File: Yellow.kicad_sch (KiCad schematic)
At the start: 15 parts

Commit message: Rename Amber to Yellow everywhere
Signed-off-by: Stefan Agner <stefan@agner.ch>
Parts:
- H5, H6: footprint Amber:DrillSlot_Plated_3.5x2.5mm -> Yellow:DrillSlot_Plated_3.5x2.5mm
- HS1: footprint Amber:Heatsink_56x56mm_2xFixation3.2mm -> Yellow:Heatsink_56x56mm_2xFixation3.2mm
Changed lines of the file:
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@@
       (effects (font (size 1.27 1.27)) (justify left))
     )
-    (property "Footprint" "Amber:DrillSlot_Plated_3.5x2.5mm" (id 2) (at 111.76 182.88 0)
+    (property "Footprint" "Yellow:DrillSlot_Plated_3.5x2.5mm" (id 2) (at 111.76 182.88 0)
       (effects (font (size 1.27 1.27)) hide)
     )
@@
       (effects (font (size 1.27 1.27)) (justify left))
     )
-    (property "Footprint" "Amber:DrillSlot_Plated_3.5x2.5mm" (id 2) (at 111.76 190.5 0)
+    (property "Footprint" "Yellow:DrillSlot_Plated_3.5x2.5mm" (id 2) (at 111.76 190.5 0)
       (effects (font (size 1.27 1.27)) hide)
     )
@@
       (effects (font (size 1.27 1.27)) (justify left))
     )
-    (property "Footprint" "Amber:Heatsink_56x56mm_2xFixation3.2mm" (id 2) (at 133.6548 185.42 0)
+    (property "Footprint" "Yellow:Heatsink_56x56mm_2xFixation3.2mm" (id 2) (at 133.6548 185.42 0)
       (effects (font (size 1.27 1.27)) hide)
     )
@@
     )
     (path "/6888556d-e390-44b5-977e-8a0092745a4b/59b3b2a4-69cc-4b91-a496-9a2aacf0b558"
-      (reference "FL1") (unit 1) (value "1k@100MHz{slash}500mA") (footprint "Amber:L_CommonModeChoke_Murata_DLW5B")
+      (reference "FL1") (unit 1) (value "1k@100MHz{slash}500mA") (footprint "Yellow:L_CommonModeChoke_Murata_DLW5B")
     )
     (path "/13673698-1ae8-48ac-89ad-67bec4817dbe"
@@
     )
     (path "/37de04fb-2d22-493d-a648-e024c9d5a4fc"
-      (reference "H5") (unit 1) (value "MountingHole") (footprint "Amber:DrillSlot_Plated_3.5x2.5mm")
+      (reference "H5") (unit 1) (value "MountingHole") (footprint "Yellow:DrillSlot_Plated_3.5x2.5mm")
     )
     (path "/bfcec0b4-32c4-4ebf-8bb4-4766287797f1"
-      (reference "H6") (unit 1) (value "MountingHole") (footprint "Amber:DrillSlot_Plated_3.5x2.5mm")
+      (reference "H6") (unit 1) (value "MountingHole") (footprint "Yellow:DrillSlot_Plated_3.5x2.5mm")
     )
     (path "/cd73f910-31d6-4226-a110-18f09eef8514"
-      (reference "HS1") (unit 1) (value "Heatsink") (footprint "Amber:Heatsink_56x56mm_2xFixation3.2mm")
+      (reference "HS1") (unit 1) (value "Heatsink") (footprint "Yellow:Heatsink_56x56mm_2xFixation3.2mm")
     )
     (path "/c7bf4e1f-6bd1-4be7-9e56-1bd438bf5d42/eda8ae3b-dbdd-4e73-8dc6-e01177bfb4f7"
-      (reference "J1") (unit 1) (value "Barrel_Jack") (footprint "Amber:BarrelJack_CUI_PJ-002A")
+      (reference "J1") (unit 1) (value "Barrel_Jack") (footprint "Yellow:BarrelJack_CUI_PJ-002A")
     )
     (path "/18c18357-12fa-4472-a108-e954e5bd7840/6dd5e861-e5d4-4759-b127-4958e3f04beb"
-      (reference "J2") (unit 1) (value "RJ45_LINK-PP_LPJG0926HENL_Horizontal") (footprint "Amber:RJ45_LINK-PP_LPJG0926HENL_Horizontal")
+      (reference "J2") (unit 1) (value "RJ45_LINK-PP_LPJG0926HENL_Horizontal") (footprint "Yellow:RJ45_LINK-PP_LPJG0926HENL_Horizontal")
     )
     (path "/aa1d8d83-5167-420c-9ee7-3e4dcc942bfc/e0469852-771a-434b-963a-8ecb4c38b617"
@@
     )
     (path "/a9e0a5b9-8f0f-46f3-b2b0-a429c678afed/45c3bea5-38ff-4276-ad09-4c18c95d656c"
-      (reference "J5") (unit 1) (value "AudioJack") (footprint "Amber:Jack_3.5mm_XKB_PJ-3270_Horizontal")
+      (reference "J5") (unit 1) (value "AudioJack") (footprint "Yellow:Jack_3.5mm_XKB_PJ-3270_Horizontal")
     )
     (path "/7c248bd3-8232-4777-a40c-eab53460cf85/fe81f5fa-e1ac-4968-a654-7214906ce5ba"
@@
     )
     (path "/a1a835e0-c072-4609-9cb4-4b95bf746f54/1247548e-da2d-4da5-8e9d-cdb0bd0eeb39"
-      (reference "J12") (unit 1) (value "Bus_M.2_Socket_M") (footprint "Amber:TE_1-2199230-3_Bus_M.2_M_H4.2mm_P0.5mm_2280_Horizontal")
+      (reference "J12") (unit 1) (value "Bus_M.2_Socket_M") (footprint "Yellow:TE_1-2199230-3_Bus_M.2_M_H4.2mm_P0.5mm_2280_Horizontal")
     )
     (path "/6888556d-e390-44b5-977e-8a0092745a4b/d2f558fb-acd9-4c71-93bb-37883bf1acff"
@@
     )
     (path "/6888556d-e390-44b5-977e-8a0092745a4b/8e4bf553-ed00-4225-96a1-870ada5deeea"
-      (reference "Q2") (unit 1) (value "BSZ440N10NS3GATMA1") (footprint "Amber:PG-TSDSON-8")
+      (reference "Q2") (unit 1) (value "BSZ440N10NS3GATMA1") (footprint "Yellow:PG-TSDSON-8")
     )
     (path "/6888556d-e390-44b5-977e-8a0092745a4b/55da7b76-bb7c-473f-a280-4b7d4142ff43"
@@
     )
     (path "/6888556d-e390-44b5-977e-8a0092745a4b/897f43a2-d08b-4609-bc6b-c864c929a423"
-      (reference "T1") (unit 1) (value "PA2467NL") (footprint "Amber:Transformer_Pulse_PA2467NL")
+      (reference "T1") (unit 1) (value "PA2467NL") (footprint "Yellow:Transformer_Pulse_PA2467NL")
     )
     (path "/7c248bd3-8232-4777-a40c-eab53460cf85/b88488bf-0e8e-4b66-85b8-98e34521bccf"
@@
     )
     (path "/7c248bd3-8232-4777-a40c-eab53460cf85/b131b144-fc54-40cc-8411-449b069a57ca"
-      (reference "U1") (unit 1) (value "RaspberryPi-CM4Lite") (footprint "Amber:RaspberryPi-CM4")
+      (reference "U1") (unit 1) (value "RaspberryPi-CM4Lite") (footprint "Yellow:RaspberryPi-CM4")
     )
     (path "/7c248bd3-8232-4777-a40c-eab53460cf85/e774090e-475c-4e3f-aa6e-6c912d7ab3b3"
-      (reference "U1") (unit 2) (value "RaspberryPi-CM4Lite") (footprint "Amber:RaspberryPi-CM4")
+      (reference "U1") (unit 2) (value "RaspberryPi-CM4Lite") (footprint "Yellow:RaspberryPi-CM4")
     )
     (path "/7c248bd3-8232-4777-a40c-eab53460cf85/4dd6bcbf-26fd-4425-8fa4-2095d8aa465e"
-      (reference "U2") (unit 1) (value "DF40C-100DS-0.4V") (footprint "Amber:Hirose_DF40_DF40C-100DS-0.4V_2x50_P0.40mm_Vertical_Virtual")
+      (reference "U2") (unit 1) (value "DF40C-100DS-0.4V") (footprint "Yellow:Hirose_DF40_DF40C-100DS-0.4V_2x50_P0.40mm_Vertical_Virtual")
     )
     (path "/7c248bd3-8232-4777-a40c-eab53460cf85/736345e1-e2da-4fe0-b090-447995db5e70"
-      (reference "U3") (unit 1) (value "DF40C-100DS-0.4V") (footprint "Amber:Hirose_DF40_DF40C-100DS-0.4V_2x50_P0.40mm_Vertical_Virtual")
+      (reference "U3") (unit 1) (value "DF40C-100DS-0.4V") (footprint "Yellow:Hirose_DF40_DF40C-100DS-0.4V_2x50_P0.40mm_Vertical_Virtual")
     )
     (path "/aa1d8d83-5167-420c-9ee7-3e4dcc942bfc/ec58ec46-77e6-4839-a341-6b0f9c76952f"
@@
     )
     (path "/12f6ca59-5dee-4aea-b4bb-e4b9cab2885b/c09bd077-0d29-41a3-91d8-7b26a3246dec"
-      (reference "U11") (unit 1) (value "SiliconLabs-MGM210P") (footprint "Amber:SiliconLabs_MGM210P")
+      (reference "U11") (unit 1) (value "SiliconLabs-MGM210P") (footprint "Yellow:SiliconLabs_MGM210P")
     )
     (path "/a9e0a5b9-8f0f-46f3-b2b0-a429c678afed/1e9ebda2-59cb-4701-873a-d55dee03ba02"

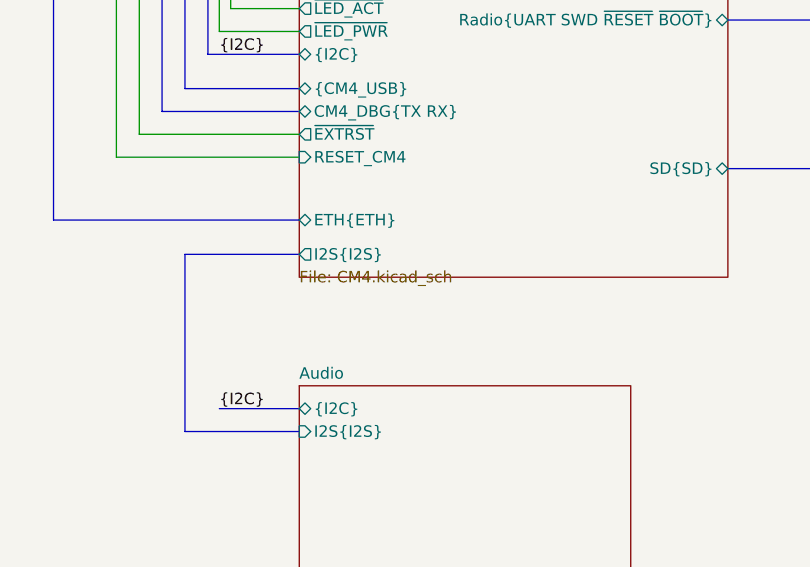
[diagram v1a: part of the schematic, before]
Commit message: Exclude TestPoints from BOM
Signed-off-by: Stefan Agner <stefan@agner.ch>
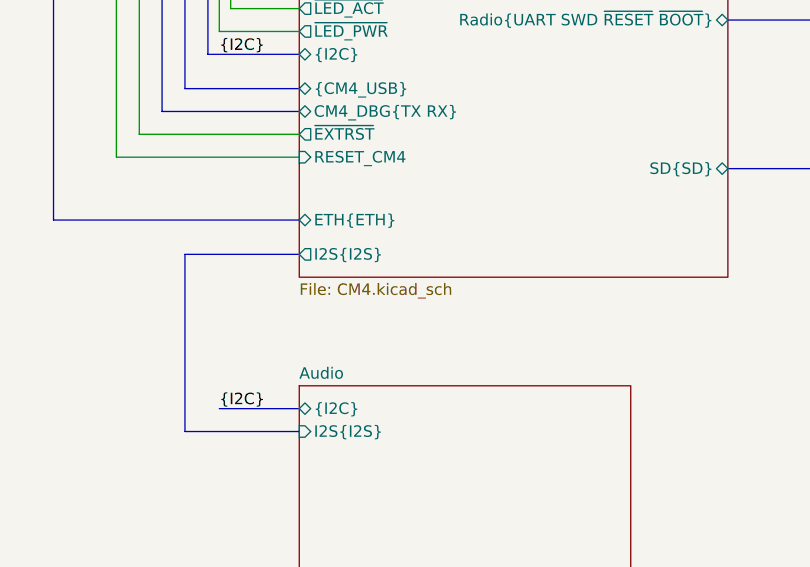
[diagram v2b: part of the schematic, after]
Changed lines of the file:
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@@
       (effects (font (size 1.27 1.27)) (justify left bottom))
     )
-    (property "Sheet file" "CM4.kicad_sch" (id 1) (at 110.49 107.8239 0)
+    (property "Sheet file" "CM4.kicad_sch" (id 1) (at 110.49 109.22 0)
       (effects (font (size 1.27 1.27)) (justify left top))
     )
